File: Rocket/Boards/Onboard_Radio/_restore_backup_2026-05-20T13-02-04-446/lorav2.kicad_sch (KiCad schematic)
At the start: 31 parts, among them J6 RFIO SMA, U2 SX1262, U3 PE4259 RF Switch, Y1 32.000MHz

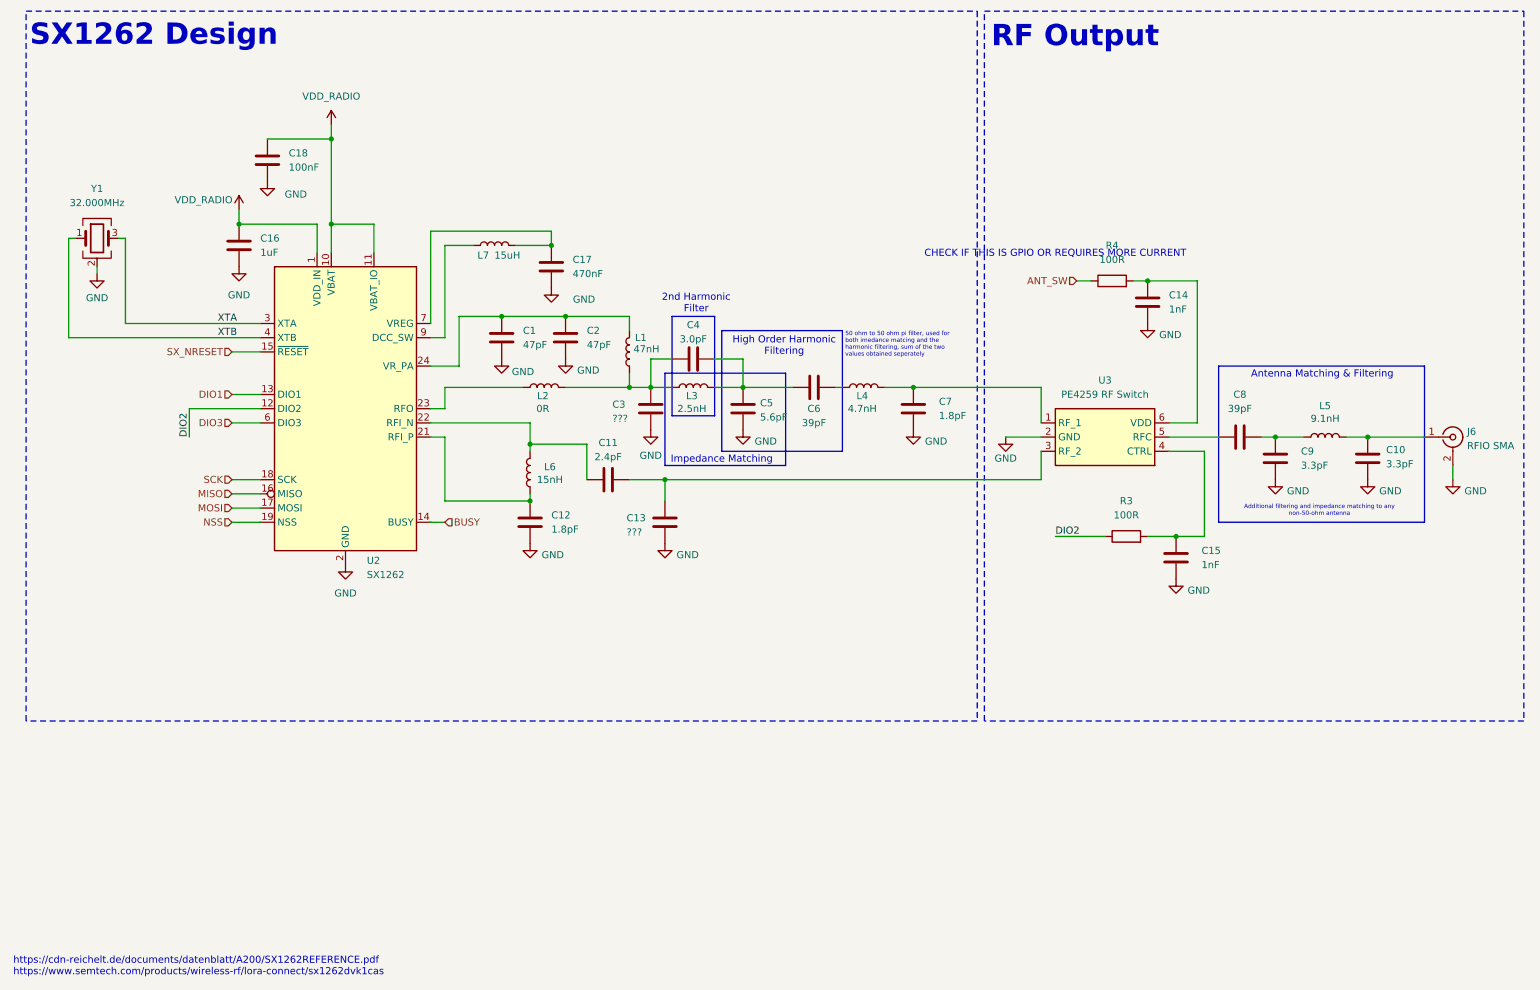
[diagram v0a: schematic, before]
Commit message: schematic bom needs updating and traces need finishing
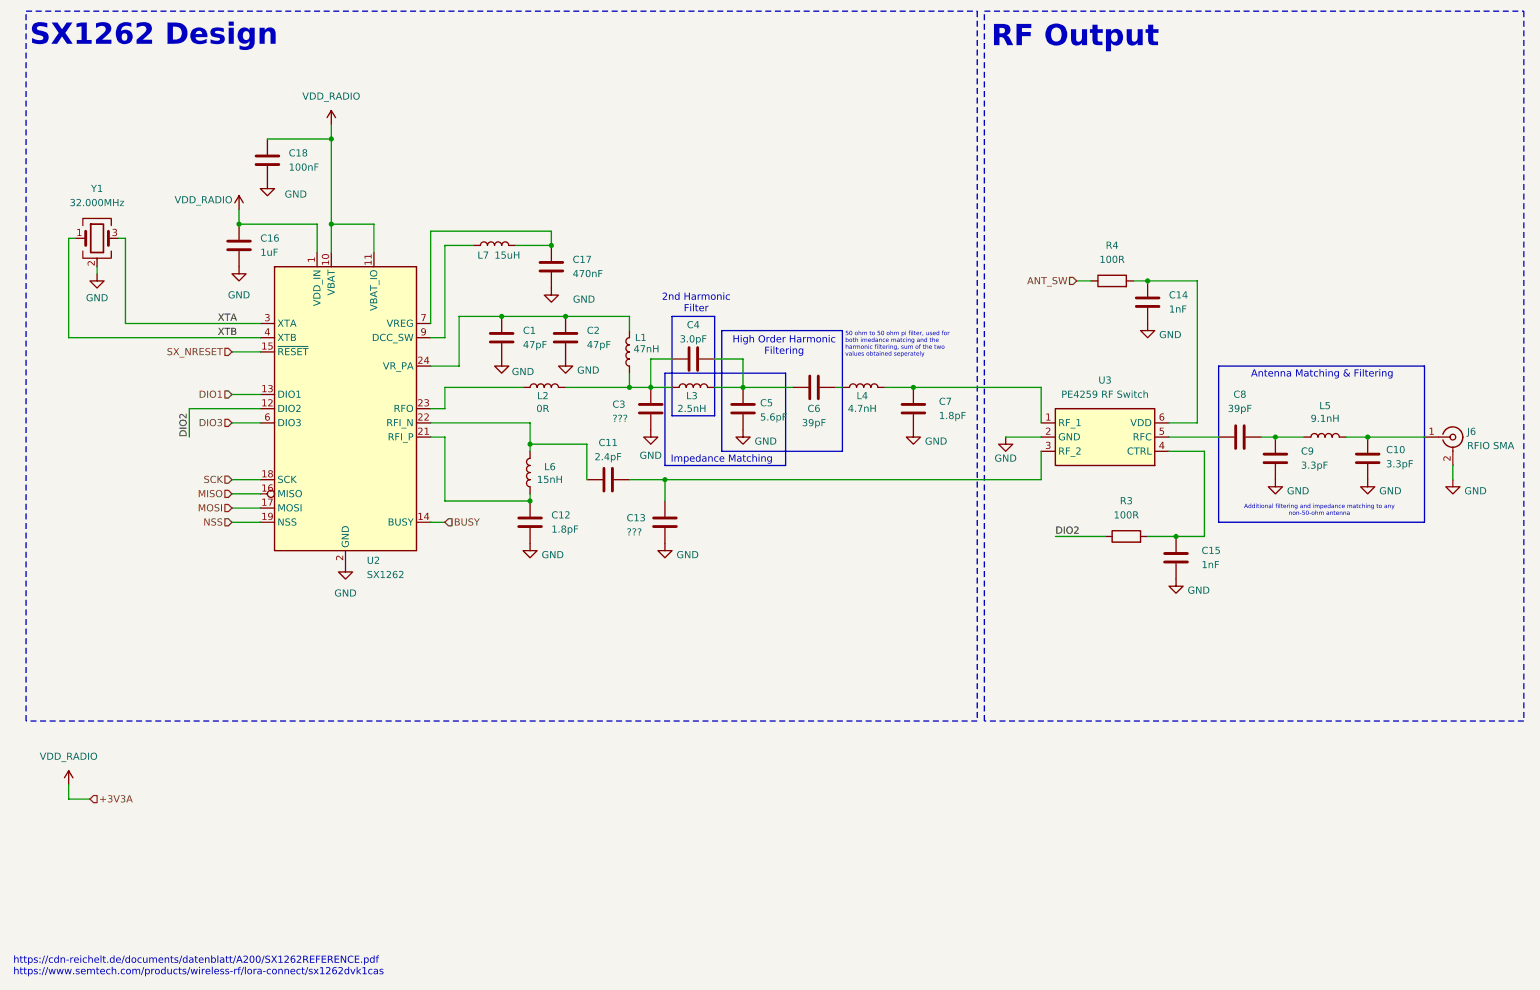
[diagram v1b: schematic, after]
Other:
- note removed: "CHECK IF THIS IS GPIO OR REQUIRES MORE CURRENT"
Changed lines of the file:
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@@
-		)
-	)
-	(text "CHECK IF THIS IS GPIO OR REQUIRES MORE CURRENT"
-		(exclude_from_sim no)
-		(at 199.39 67.564 0)
-		(effects
-			(font
-				(size 1.27 1.27)
-			)
 		)
 	)
@@
 	(wire
 		(pts
+			(xy 22.86 165.1) (xy 26.67 165.1)
+		)
+		(stroke
+			(width 0)
+			(type default)
+		)
+	)
+	(wire
+		(pts
 			(xy 105.41 111.76) (xy 105.41 110.49)
 		)
@@
 		(pts
 			(xy 196.85 97.79) (xy 196.85 91.44)
+		)
+		(stroke
+			(width 0)
+			(type default)
+		)
+	)
+	(wire
+		(pts
+			(xy 22.86 162.56) (xy 22.86 165.1)
 		)
 		(stroke
@@
 			)
 			(justify right)
+		)
+	)
+	(hierarchical_label "+3V3A"
+		(shape input)
+		(at 26.67 165.1 0)
+		(effects
+			(font
+				(size 1.27 1.27)
+			)
+			(justify left)
 		)
 	)
@@
 					(unit 1)
 				)
+			)
+		)
+	)
+	(symbol
+		(lib_id "power:+3V3")
+		(at 22.86 162.56 0)
+		(unit 1)
+		(body_style 1)
+		(exclude_from_sim no)
+		(in_bom yes)
+		(on_board yes)
+		(in_pos_files yes)
+		(dnp no)
+		(fields_autoplaced yes)
+		(property "Reference" "#PWR076"
+			(at 22.86 166.37 0)
+			(hide yes)
+			(show_name no)
+			(do_not_autoplace no)
+			(effects
+				(font
+					(size 1.27 1.27)
+				)
+			)
+		)
+		(property "Value" "VDD_RADIO"
+			(at 22.86 157.48 0)
+			(show_name no)
+			(do_not_autoplace no)
+			(effects
+				(font
+					(size 1.27 1.27)
+				)
+			)
+		)
+		(property "Footprint" ""
+			(at 22.86 162.56 0)
+			(hide yes)
+			(show_name no)
+			(do_not_autoplace no)
+			(effects
+				(font
+					(size 1.27 1.27)
+				)
+			)
+		)
+		(property "Datasheet" ""
+			(at 22.86 162.56 0)
+			(hide yes)
+			(show_name no)
+			(do_not_autoplace no)
+			(effects
+				(font
+					(size 1.27 1.27)
+				)
+			)
+		)
+		(property "Description" "Power symbol creates a global label with name \"+3V3\""
+			(at 22.86 162.56 0)
+			(hide yes)
+			(show_name no)
+			(do_not_autoplace no)
+			(effects
+				(font
+					(size 1.27 1.27)
+				)
+			)
+		)
+		(pin "1"
+		)
+		(instances
+			(project "rf_rocket_module"
+				(path "/4940ffbe-f45f-4917-a247-12e2b32b6c35/ec17b761-2334-4457-8873-4c3a71db4204"
+					(reference "#PWR076")
+					(unit 1)
+				)
